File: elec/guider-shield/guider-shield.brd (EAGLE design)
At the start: 35.6 x 27.9 mm, 11 parts, among them U2 PCA9536-SO8, U3 TLP291, X1 OPENMV3, X2 MTJ-663X1

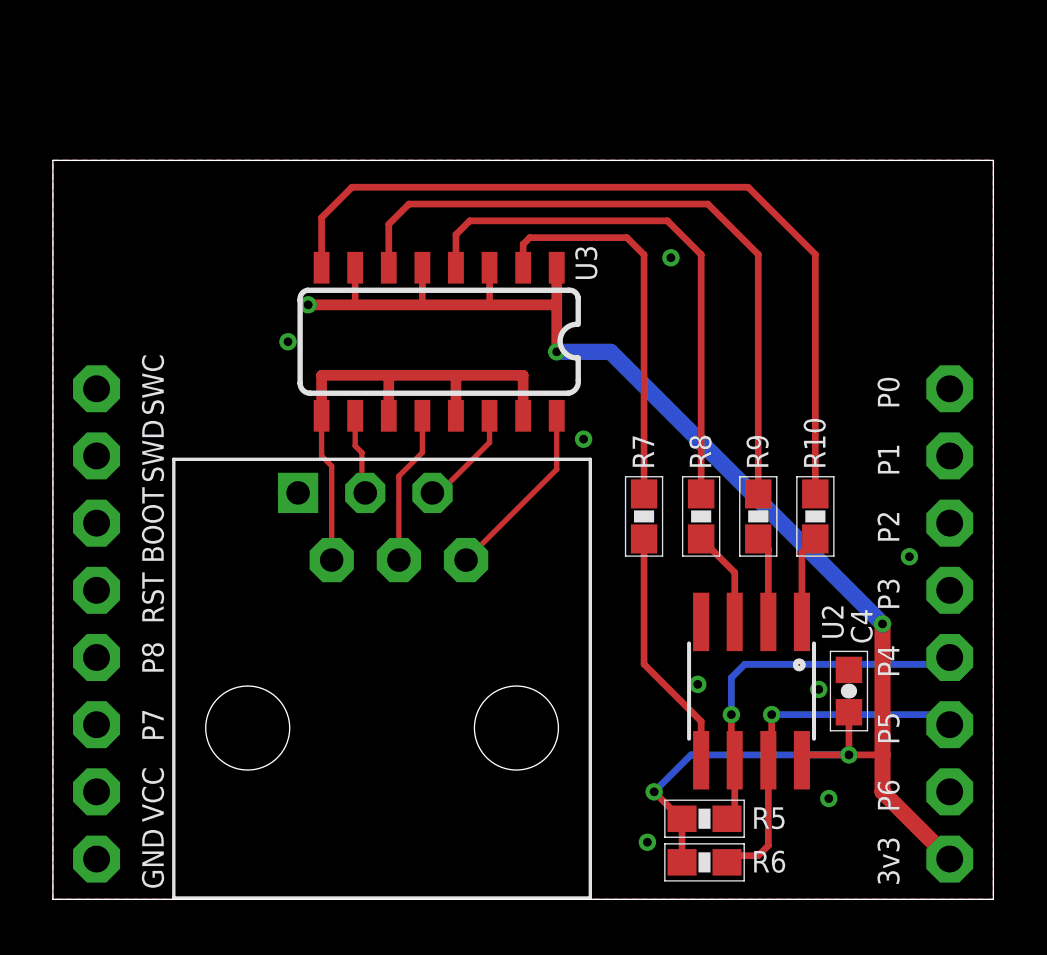
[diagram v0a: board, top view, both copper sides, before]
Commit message: guider-shield added intervalometer output
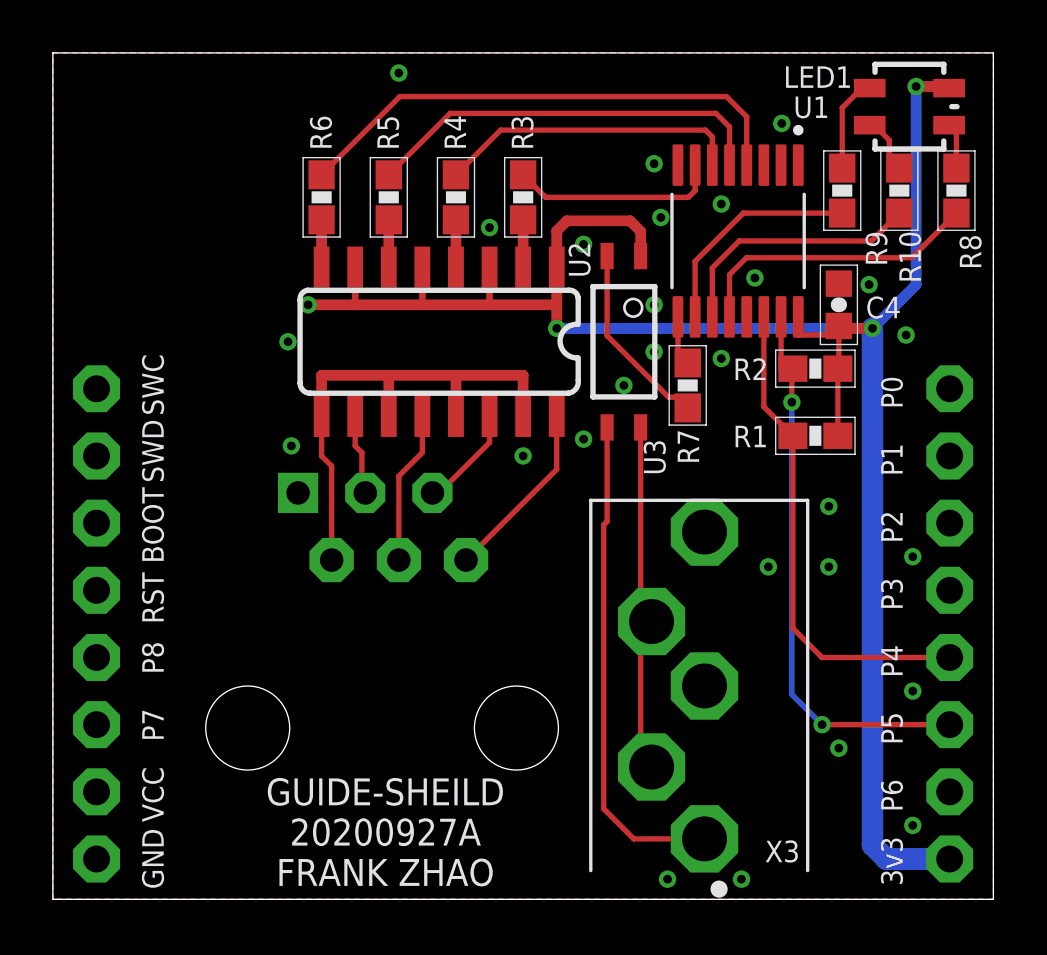
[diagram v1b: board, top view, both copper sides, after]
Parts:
- added LED1: LED-TRICOLOR, guider-shield:LED-TRICOLOR-SMD
- added R1, R2: 4K7, sfe:0603-RES
- added R3, R4: 220R, sfe:0603-RES
- added U1: PCA9554PW, guider-shield:SOP65P640X120-16N
- added X3: SJ1-3535N, guider-shield:CUI_SJ1-3535N
- R5, R6: value 4K7 -> 220R
- U2: value PCA9536-SO8 -> TLP291; device guider-shield:SO08 -> guider-shield:SO016
- U3: value TLP291 -> TLP283; device guider-shield:SO016 -> guider-shield:MINI-FLAT-4
- moved R6 29.0 mm to (10.2, 26.5), turned to 90 degrees
- moved R5 26.4 mm to (12.7, 26.5), turned to 90 degrees
- moved U2 17.7 mm to (14.6, 21.1)
- moved R8 15.6 mm to (34.2, 26.8)
- moved C4 14.6 mm to (29.7, 22.5)
- moved R10 12.7 mm to (32.0, 26.8)
- moved R9 12.7 mm to (29.8, 26.8)
- moved U3 6.98 mm to (21.6, 21.1), turned to 270 degrees
- moved R7 5.22 mm to (24.0, 19.4), turned to 90 degrees
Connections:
- removed net N$22: R9.2, U2.2
- removed net N$23: R10.2, U2.1
- new net IO-0: R6.2, U1.4
- new net IO-1: R5.2, U1.5
- new net IO-2: R4.2, U1.6
- new net IO-3: R3.2, U1.7
- new net IO-4: R7.2, U1.9
- new net IO-5: R9.2, U1.10
- new net IO-6: R10.2, U1.11
- new net IO-7: R8.2, U1.12
- new net N$14: U3.3, X3.1
- new net N$15: U3.4, X3.2, X3.3
- new net N$4: LED1.G, R10.1
- new net N$8: R3.1, U2.2
- net 3V3: now also LED1.A, R1.2, R2.2, U1.16, U2.1, U2.3, U2.5, U2.7; no longer R5.2, R6.2, U2.8, U3.3, U3.5, U3.7
- net EAST: now also U2.10; no longer U3.10
- net GND: now also U1.1, U1.2, U1.3, U1.8; no longer U2.4
- net N$1: now also LED1.R, R8.1; no longer R7.2, U2.5
- net N$16: now also R4.1, U2.4; no longer R8.1, U3.4
- net N$2: now also LED1.B, R9.1; no longer R8.2, U2.3
- net N$20: now also R5.1, U2.6; no longer R9.1, U3.6
- net N$21: now also R6.1, U2.8; no longer R10.1, U3.8
- net N$24: now also U2.11, U2.13, U2.15, U2.9; no longer U3.11, U3.13, U3.15, U3.9
- net NORTH: now also U2.12; no longer U3.12
- net SCL: now also R1.1, U1.14; no longer R5.1, U2.6
- net SDA: now also R2.1, U1.15; no longer R6.1, U2.7
- net SOUTH: now also U2.14; no longer U3.14
- net WEST: now also U2.16; no longer U3.16
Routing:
- net N$21: track 31.1 -> 1.81 mm
- net N$20: track 25.8 -> 1.81 mm
- net IO-0: track 0.00 -> 19.4 mm
- net N$14: track 0.00 -> 18.8 mm
- net N$16: track 20.3 -> 1.81 mm
- net 3V3: track 59.2 -> 75.6 mm, vias 5 -> 4
- net IO-1: track 0.00 -> 15.5 mm
- net N$15: track 0.00 -> 13.4 mm
- net IO-2: track 0.00 -> 11.6 mm
- net IO-7: track 0.00 -> 11.1 mm
- net IO-6: track 0.00 -> 9.78 mm
- net IO-5: track 0.00 -> 8.42 mm
- net IO-3: track 0.00 -> 7.92 mm
- net N$13: track 14.9 -> 7.43 mm
- net N$1: track 9.26 -> 1.90 mm
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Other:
- board size 35.6 x 27.9 mm -> 35.6 x 32 mm
- board text added: "GUIDE-SHEILD 20200927A FRANK ZHAO"
